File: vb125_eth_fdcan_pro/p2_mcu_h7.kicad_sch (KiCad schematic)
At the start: 62 parts, among them J1 MEM2061-01-188-00-A, J2 TAGconnect NL, J3 Conn_02x20_Pin, M1 DM-OLED042-647, SW1 KSS331GLFS, U1 STM32H725IGKx, X1 ECX-.327-CDX-1293

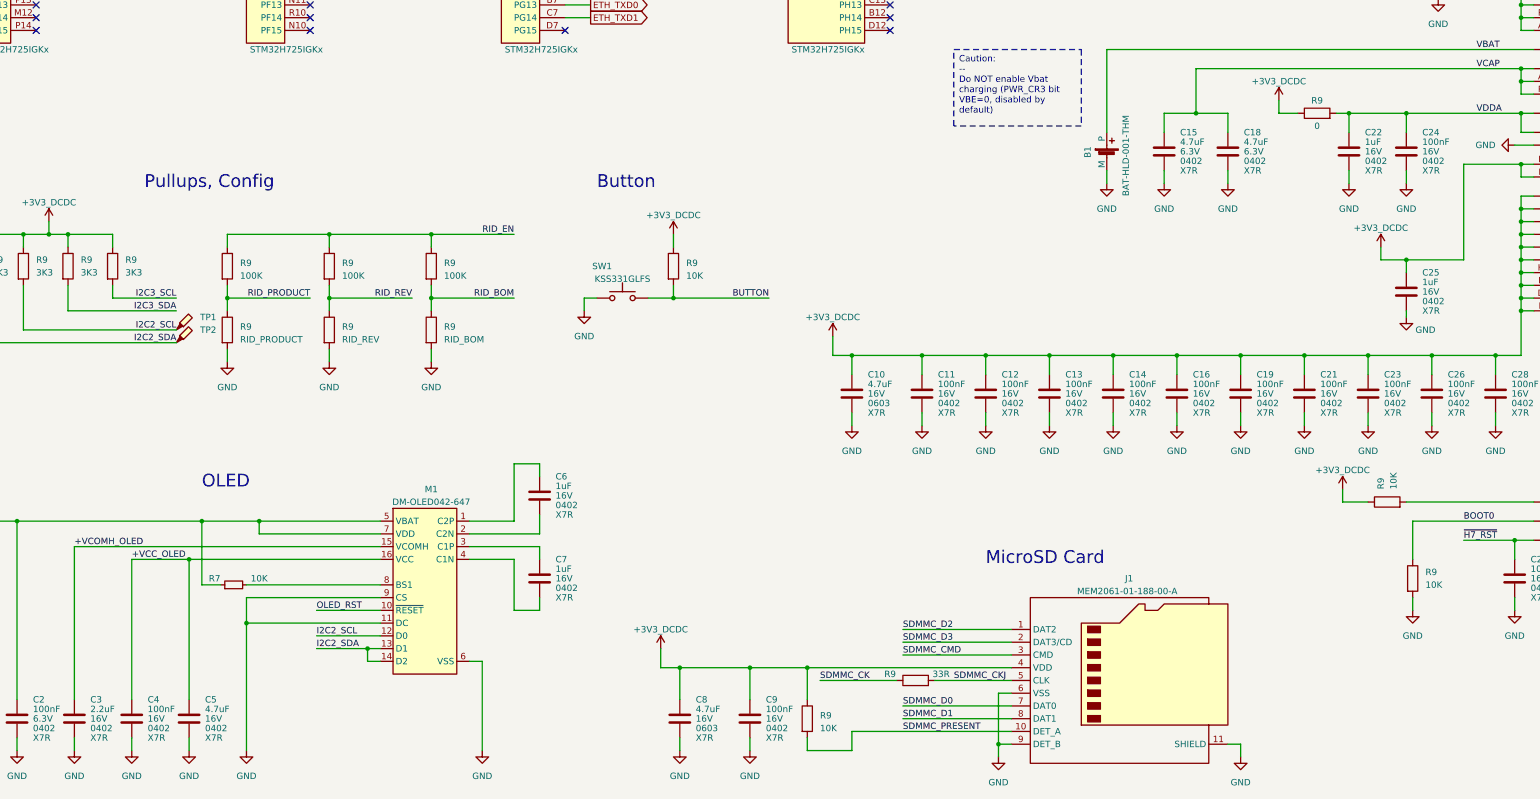
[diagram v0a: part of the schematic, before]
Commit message: Selection of capacitors for VB125
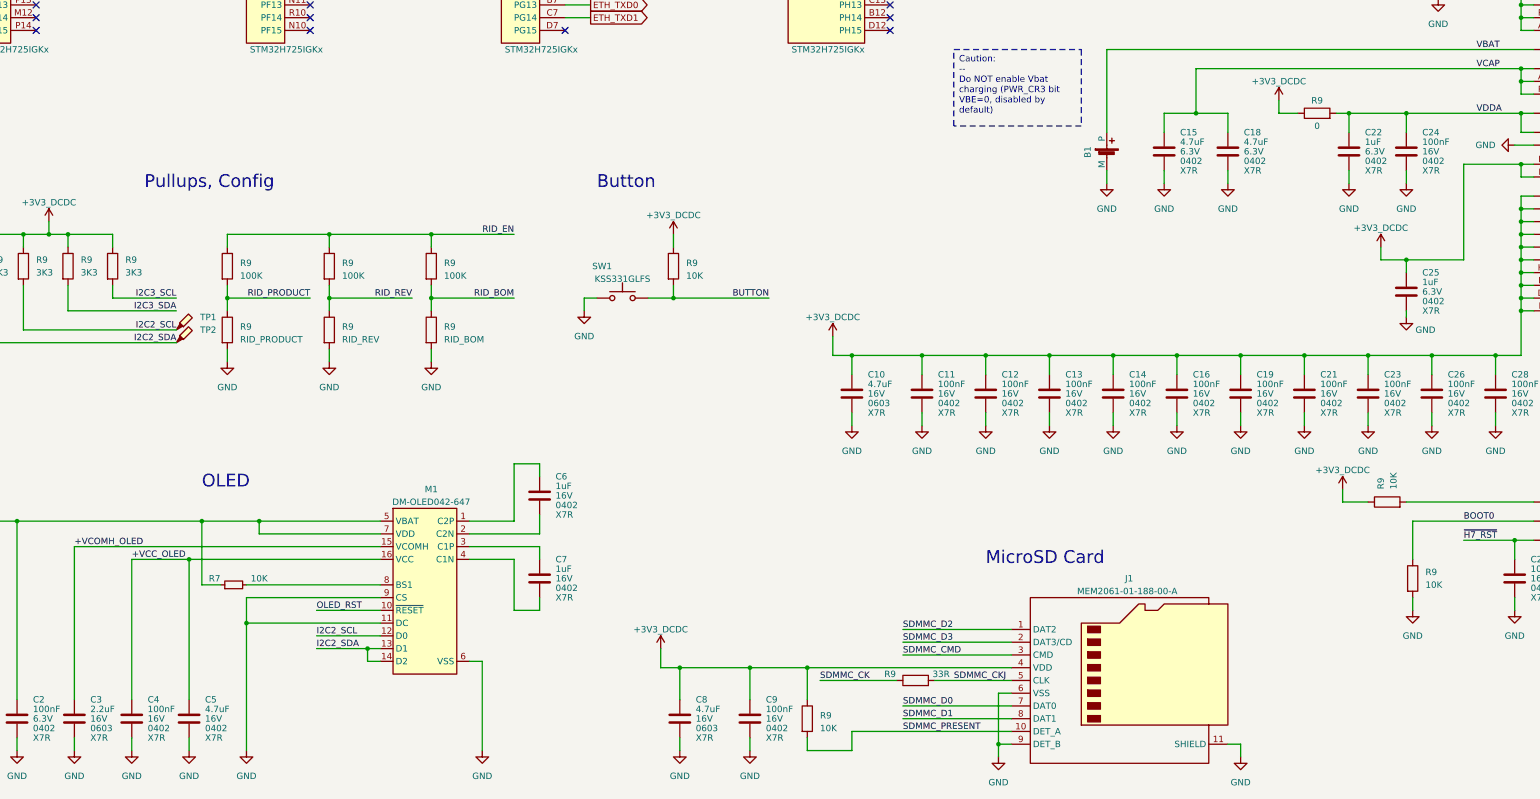
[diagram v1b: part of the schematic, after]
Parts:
- B1: value BAT-HLD-001-THM -> (none)
- C1, C15, C18: Mpn1 (none) -> 06036C475KAT2A; Mpn2 (none) -> ТОЛЬКО ОДИН ПРОИЗВОДИТ. В КОРПУСЕ 0603
- C10, C8: Mpn1 (none) -> Murata:GRM188Z71C475KE21J; Mpn2 (none) -> Murata:GRM188Z71C475KE21D
- C11, C12, C13, C14, C16, C19, C2, C21, C23, C24, C26, C28, C29, C4, C9: Mpn1 (none) -> Samsung:CL05B104KQ5NNNC; Mpn2 (none) -> YAGEO:CC0402KRX7R5BB104
- C17, C20: Mpn1 (none) -> 04025A120KAT2A; Mpn2 (none) -> C0402C120K5GAC7867
- C22, C25: Mpn1 (none) -> Murata:GRM155R70J105KA12D; Mpn2 (none) -> Murata:GRM155R70J105KA12J; Voltage 16V -> 6.3V
- C27, C31: Mpn2 (none) -> - СМОТРЕЛ, В НАЛИЧИИ НЕТ ТАКИХ
- C3: footprint Capacitor_SMD:C_0402_1005Metric -> Capacitor_SMD:C_0603_1608Metric; Mpn1 (none) -> Murata:GRM188Z71C225KE43D; Mpn2 (none) -> Taiyo Yuden:EMK107BB7225KA-T; Package 0402 -> 0603
- C30: Mpn1 (none) -> CC0402KRNPO9BN221; Mpn2 (none) -> C0402C221K5GAC7867
- C6, C7: Mpn1 (none) -> -- mixed values --CL10B105KO8NNNC только В КОРПУСЕ 0603 и б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; Mpn2 (none) -> -- mixed values -- C0603C105K4RAC7867 только В КОРПУСЕ 0603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

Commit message: Add missing footprints, ready to layout.
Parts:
- L1: footprint (none) -> vhrd_inductor:MURATA_LQM2
- X1: footprint vhrd_cristal:ECX-.327-CDX-1293 -> vhrd_crystal:ECX-.327-CDX-1293
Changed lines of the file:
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@@
       (effects (font (size 1.27 1.27)))
     )
-    (property "Footprint" "" (at 387.35 118.11 0)
-      (effects (font (size 1.27 1.27)) hide)
-    )
-    (property "Datasheet" "~" (at 387.35 118.11 0)
+    (property "Footprint" "vhrd_inductor:MURATA_LQM2" (at 387.35 118.11 0)
+      (effects (font (size 1.27 1.27)) hide)
+    )
+    (property "Datasheet" "https://search.murata.co.jp/Ceramy/image/img/P02/JELF243B-0022.pdf" (at 387.35 118.11 0)
       (effects (font (size 1.27 1.27)) hide)
     )
@@
       (effects (font (size 1.27 1.27)))
     )
-    (property "Footprint" "vhrd_cristal:ECX-.327-CDX-1293" (at 281.94 38.1 0)
-      (effects (font (size 1.27 1.27)) hide)
-    )
-    (property "Datasheet" "~https://ecsxtal.com/store/pdf/ECX-.327-CDX-1293.pdf" (at 281.94 35.56 0)
-      (effects (font (size 1.27 1.27)) hide)
-    )
+    (property "Footprint" "vhrd_crystal:ECX-.327-CDX-1293" (at 281.94 38.1 0)
+      (effects (font (size 1.27 1.27)) hide)
+    )
+    (property "Datasheet" "https://ecsxtal.com/store/pdf/ECX-.327-CDX-1293.pdf" (at 281.94 35.56 0)
+      (effects (font (size 1.27 1.27)) hide)
+    )

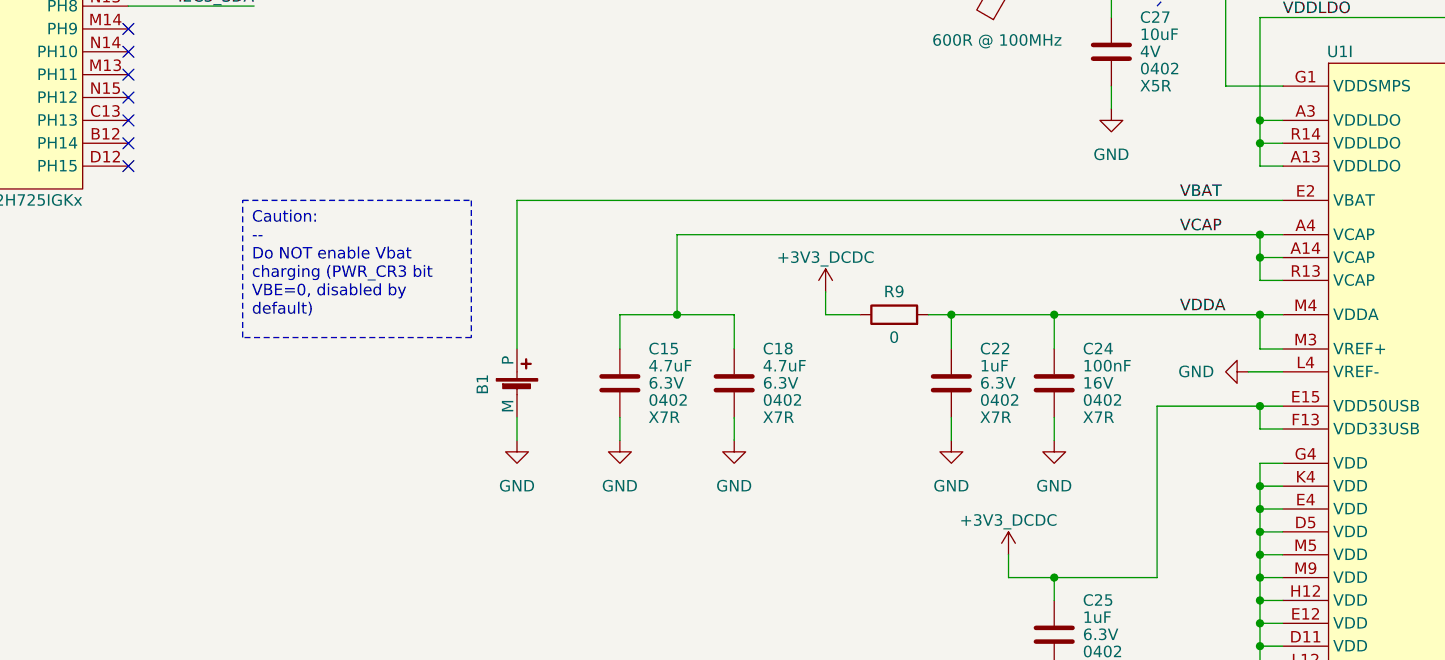
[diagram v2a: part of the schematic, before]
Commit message: Preliminary placement.
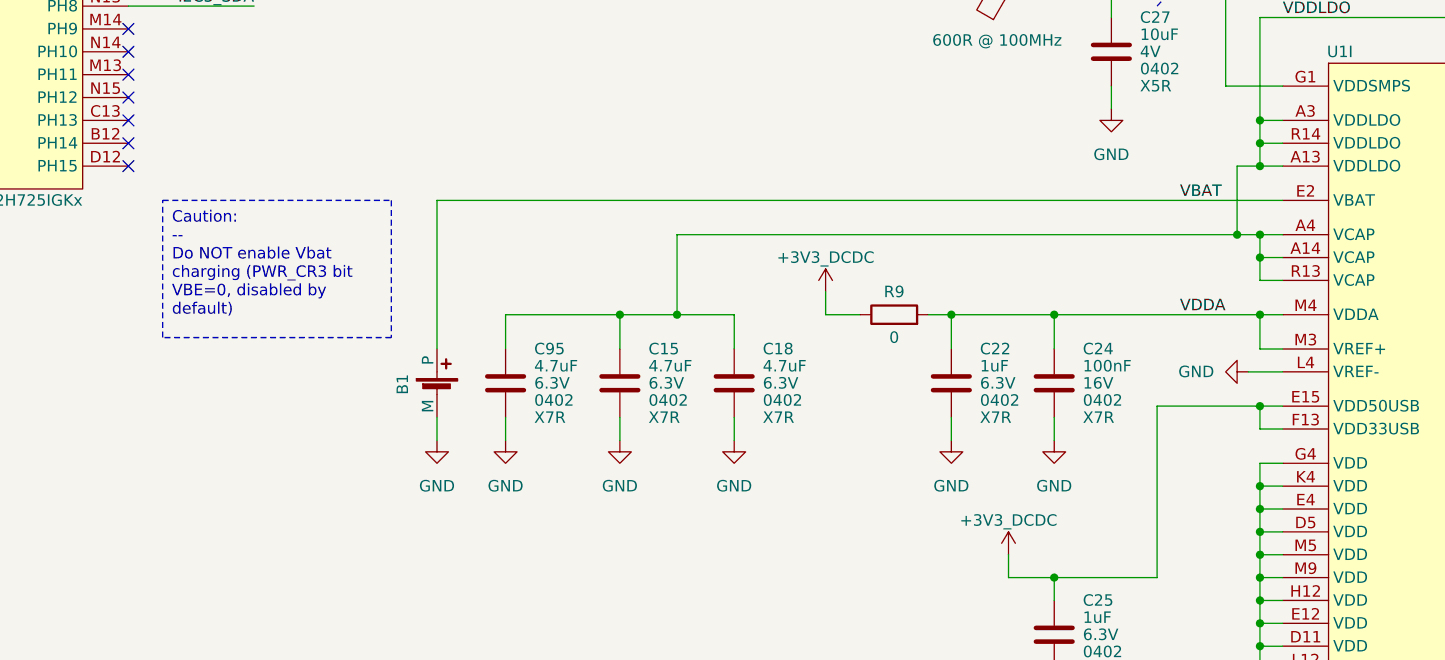
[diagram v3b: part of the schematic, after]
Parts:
- added C95: 4.7uF, Capacitor_SMD:C_0402_1005Metric, symbol Device:C
- M1: footprint vhrd_opto_display:DM-OLED042-647 -> vhrd_opto_display:DM-OLED042-647-TOP
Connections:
- net VCAP is gone; now on net VDDLDO: C15.1, C18.1, U1.A14 (VCAP), U1.A4 (VCAP), U1.R13 (VCAP)
- net GND: now also C95.2
- net VDDLDO: now also C95.1
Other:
- moved on the sheet: B1
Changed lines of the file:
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@@
   (junction (at 311.15 143.51) (diameter 0) (color 0 0 0 0)
   )
+  (junction (at 334.01 127) (diameter 0) (color 0 0 0 0)
+  )
   (junction (at 278.13 191.77) (diameter 0) (color 0 0 0 0)
   )
@@
   (junction (at 350.52 67.31) (diameter 0) (color 0 0 0 0)
   )
+  (junction (at 331.47 134.62) (diameter 0) (color 0 0 0 0)
+  )
   (junction (at 374.65 132.08) (diameter 0) (color 0 0 0 0)
   )
@@
   (junction (at 374.65 200.66) (diameter 0) (color 0 0 0 0)
   )
+  (junction (at 262.89 143.51) (diameter 0) (color 0 0 0 0)
+  )
   (junction (at 334.01 170.18) (diameter 0) (color 0 0 0 0)
   )
@@
     (stroke (width 0) (type default))
   )
+  (wire (pts (xy 250.19 147.32) (xy 250.19 143.51))
+    (stroke (width 0) (type default))
+  )
   (wire (pts (xy 208.28 106.68) (xy 222.25 106.68))
     (stroke (width 0) (type default))
@@
     (stroke (width 0) (type default))
   )
+  (wire (pts (xy 331.47 127) (xy 334.01 127))
+    (stroke (width 0) (type default))
+  )
   (wire (pts (xy 80.01 270.51) (xy 80.01 245.11))
     (stroke (width 0) (type default))
@@
     (stroke (width 0) (type default))
   )
-  (wire (pts (xy 269.24 134.62) (xy 334.01 134.62))
+  (wire (pts (xy 269.24 134.62) (xy 331.47 134.62))
     (stroke (width 0) (type default))
   )
@@
     (stroke (width 0) (type default))
   )
-  (wire (pts (xy 251.46 154.94) (xy 251.46 157.48))
+  (wire (pts (xy 242.57 154.94) (xy 242.57 157.48))
     (stroke (width 0) (type default))
   )
@@
     (stroke (width 0) (type default))
   )
+  (wire (pts (xy 331.47 134.62) (xy 331.47 127))
+    (stroke (width 0) (type default))
+  )
   (wire (pts (xy 38.1 43.18) (xy 71.12 43.18))
     (stroke (width 0) (type default))
@@
     (stroke (width 0) (type default))
   )
-  (wire (pts (xy 251.46 130.81) (xy 336.55 130.81))
+  (wire (pts (xy 242.57 130.81) (xy 336.55 130.81))
     (stroke (width 0) (type default))
   )
@@
     (stroke (width 0) (type default))
   )
+  (wire (pts (xy 250.19 154.94) (xy 250.19 157.48))
+    (stroke (width 0) (type default))
+  )
   (wire (pts (xy 334.01 165.1) (xy 336.55 165.1))
     (stroke (width 0) (type default))
@@
     (stroke (width 0) (type default))
   )
+  (wire (pts (xy 331.47 134.62) (xy 334.01 134.62))
+    (stroke (width 0) (type default))
+  )
   (wire (pts (xy 374.65 139.7) (xy 374.65 137.16))
     (stroke (width 0) (type default))
@@
     (stroke (width 0) (type default))
   )
-  (wire (pts (xy 251.46 130.81) (xy 251.46 147.32))
+  (wire (pts (xy 242.57 130.81) (xy 242.57 147.32))
     (stroke (width 0) (type default))
   )
@@
     (stroke (width 0) (type default))
   )
+  (wire (pts (xy 250.19 143.51) (xy 262.89 143.51))
+    (stroke (width 0) (type default))
+  )
   (wire (pts (xy 273.05 33.02) (xy 273.05 30.48))
     (stroke (width 0) (type default))
@@
   )
   (text_box "Caution:\n--\nDo NOT enable Vbat charging (PWR_CR3 bit VBE=0, disabled by default)"
-    (at 220.98 130.81 0) (size 25.4 15.24)
+    (at 212.09 130.81 0) (size 25.4 15.24)
     (stroke (width 0.1524) (type dash) (color 194 194 0 1))
     (fill (type none))
@@
     (effects (font (size 1.27 1.27) (color 194 0 194 1)) (justify right bottom))
   )
-  (label "VCAP" (at 325.12 134.62 0) (fields_autoplaced)
-    (effects (font (size 1.27 1.27)) (justify left bottom))
-  )
   (label "SPI1_SCK" (at 125.73 35.56 180) (fields_autoplaced)
     (effects (font (size 1.27 1.27) (color 194 0 194 1)) (justify right bottom))
@@
     )
   )
-  (symbol (lib_id "power:GND") (at 251.46 157.48 0) (unit 1)
+  (symbol (lib_id "power:GND") (at 250.19 157.48 0) (unit 1)
+    (in_bom yes) (on_board yes) (dnp no) (fields_autoplaced)
+    (property "Reference" "#PWR09" (at 250.19 163.83 0)
+      (effects (font (size 1.27 1.27)) hide)
+    )
+    (property "Value" "GND" (at 250.19 162.56 0)
+      (effects (font (size 1.27 1.27)))
+    )
+    (property "Footprint" "" (at 250.19 157.48 0)
+      (effects (font (size 1.27 1.27)) hide)
+    )
+    (property "Datasheet" "" (at 250.19 157.48 0)
+      (effects (font (size 1.27 1.27)) hide)
+    )
+    (pin "1")
+    (instances
+      (project "vb125_eth_fdcan_pro"
+        (path "/b473bccb-f14c-41d5-b473-137d3ef8ae1e/c16e79c7-955f-4686-8fe9-acff02e57751"
+          (reference "#PWR09") (unit 1)
+        )
+      )
+    )
+  )
+  (symbol (lib_id "power:GND") (at 242.57 157.48 0) (unit 1)
     (in_bom yes) (on_board yes) (dnp no) (fields_autoplaced)
-    (property "Reference" "#PWR028" (at 251.46 163.83 0)
+    (property "Reference" "#PWR028" (at 242.57 163.83 0)
       (effects (font (size 1.27 1.27)) hide)
     )
-    (property "Value" "GND" (at 251.46 162.56 0)
+    (property "Value" "GND" (at 242.57 162.56 0)
       (effects (font (size 1.27 1.27)))
     )
-    (property "Footprint" "" (at 251.46 157.48 0)
+    (property "Footprint" "" (at 242.57 157.48 0)
       (effects (font (size 1.27 1.27)) hide)
     )
-    (property "Datasheet" "" (at 251.46 157.48 0)
+    (property "Datasheet" "" (at 242.57 157.48 0)
       (effects (font (size 1.27 1.27)) hide)
     )
@@
       (effects (font (size 1.27 1.27)))
     )
-    (property "Footprint" "vhrd_opto_display:DM-OLED042-647" (at 109.22 222.25 0)
+    (property "Footprint" "vhrd_opto_display:DM-OLED042-647-TOP" (at 109.22 222.25 0)
       (effects (font (size 1.27 1.27)) hide)
     )
-    (property "Datasheet" "https://drive.google.com/file/d/1ygmyopC3FinO5EHa4Gdgm3Pccdjo0d4R/view" (at 119.38 257.81 0)
+    (property "Datasheet" "https://cdn.shopify.com/s/files/1/0264/7629/files/DM-OLED042-647_Datasheet_172e9a12-376c-4f72-95bb-83c6a7033324.pdf?v=1675320439" (at 119.38 257.81 0)
       (effects (font (size 1.27 1.27)) hide)
     )
@@
     )
   )
+  (symbol (lib_id "Device:C") (at 250.19 151.13 0) (unit 1)
+    (in_bom yes) (on_board yes) (dnp no)
+    (property "Reference" "C95" (at 253.365 147.32 0)
+      (effects (font (size 1.27 1.27)) (justify left))
+    )
+    (property "Value" "4.7uF" (at 253.365 149.225 0)
+      (effects (font (size 1.27 1.27)) (justify left))
+    )
+    (property "Footprint" "Capacitor_SMD:C_0402_1005Metric" (at 251.1552 154.94 0)
+      (effects (font (size 1.27 1.27)) hide)
+    )
+    (property "Datasheet" "~" (at 250.19 151.13 0)
+      (effects (font (size 1.27 1.27)) hide)
+    )
+    (property "Voltage" "6.3V" (at 253.365 151.13 0)
+      (effects (font (size 1.27 1.27)) (justify left))
+    )
+    (property "Dielectric" "X7R" (at 253.365 154.94 0)
+      (effects (font (size 1.27 1.27)) (justify left))
+    )
+    (property "Package" "0402" (at 253.365 153.035 0)
+      (effects (font (size 1.27 1.27)) (justify left))
+    )
+    (property "Vworking" "?" (at 250.19 151.13 0)
+      (effects (font (size 1.27 1.27)) hide)
+    )
+    (property "Mpn1" "06036C475KAT2A" (at 250.19 151.13 0)
+      (effects (font (size 1.27 1.27)) hide)
+    )
+    (property "Mpn2" "ТОЛЬКО ОДИН ПРОИЗВОДИТ. В КОРПУСЕ 0603" (at 250.19 151.13 0)
+      (effects (font (size 1.27 1.27)) hide)
+    )
+    (pin "1")
+    (pin "2")
+    (instances
+      (project "vb125_eth_fdcan_pro"
+        (path "/b473bccb-f14c-41d5-b473-137d3ef8ae1e/c16e79c7-955f-4686-8fe9-acff02e57751"
+          (reference "C95") (unit 1)
+        )
+      )
+    )
+  )
   (symbol (lib_id "power:GND") (at 180.34 270.51 0) (unit 1)
     (in_bom yes) (on_board yes) (dnp no) (fields_autoplaced)
@@
     )
   )
-  (symbol (lib_id "vhrd_connector_battery:BAT-HLD-001-THM") (at 251.46 152.4 0) (unit 1)
+  (symbol (lib_id "vhrd_connector_battery:BAT-HLD-001-THM") (at 242.57 152.4 0) (unit 1)
     (in_bom yes) (on_board yes) (dnp no)
-    (property "Reference" "B1" (at 247.65 152.4 90)
+    (property "Reference" "B1" (at 238.76 152.4 90)
       (effects (font (size 1.27 1.27)) (justify left))
     )
-    (property "Value" " " (at 255.27 160.02 90)
+    (property "Value" " " (at 246.38 160.02 90)
       (effects (font (size 1.27 1.27)) (justify left))
     )
-    (property "Footprint" "vhrd_connector_battery:BAT-HLD-001-THM" (at 251.46 152.4 0)
+    (property "Footprint" "vhrd_connector_battery:BAT-HLD-001-THM" (at 242.57 152.4 0)
       (effects (font (size 1.27 1.27)) hide)
     )
-    (property "Datasheet" "~https://linxtechnologies.com/wp/wp-content/uploads/bat-hld-001-thm.pdf" (at 251.46 152.4 0)
+    (property "Datasheet" "~https://linxtechnologies.com/wp/wp-content/uploads/bat-hld-001-thm.pdf" (at 242.57 152.4 0)
       (effects (font (size 1.27 1.27)) hide)
     )

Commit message: Continue with floorplan
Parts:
- removed SW1: KSS331GLFS, vhrd_electromechanical:SW_KSS3, symbol Switch:SW_Push
- added VB125C1: vb125c1_button_board, vhrd_boards:vb125c1_button_board, symbol vhrd_boards:vb125c1_button_board
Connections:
- net BUTTON: now also VB125C1.2
- net GND: now also VB125C1.1
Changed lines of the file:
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@@
-    )
-  )
-  (symbol (lib_id "Switch:SW_Push") (at 154.94 180.34 0) (unit 1)
-    (in_bom yes) (on_board yes) (dnp no) (fields_autoplaced)
-    (property "Reference" "SW1" (at 148.9117 173.99 0)
-      (effects (font (size 1.27 1.27)) (justify left))
-    )
-    (property "Value" "KSS331GLFS" (at 154.94 176.53 0)
-      (effects (font (size 1.27 1.27)))
-    )
-    (property "Footprint" "vhrd_electromechanical:SW_KSS3" (at 154.94 175.26 0)
-      (effects (font (size 1.27 1.27)) hide)
-    )
-    (property "Datasheet" "~" (at 154.94 175.26 0)
-      (effects (font (size 1.27 1.27)) hide)
-    )
-    (pin "1")
-    (pin "2")
-    (instances
-      (project "vb125_eth_fdcan_pro"
-        (path "/b473bccb-f14c-41d5-b473-137d3ef8ae1e/c16e79c7-955f-4686-8fe9-acff02e57751"
-          (reference "SW1") (unit 1)
-        )
-      )
     )
   )
@@
         )
       )
+    )
+  )
+  (symbol (lib_id "vhrd_boards:vb125c1_button_board") (at 154.94 180.34 0) (unit 1)
+    (in_bom yes) (on_board yes) (dnp no)
+    (property "Reference" "VB125C1" (at 154.94 175.26 0)
+      (effects (font (size 1.27 1.27)))
+    )
+    (property "Value" "vb125c1_button_board" (at 160.02 182.88 0)
+      (effects (font (size 1.27 1.27)))
+    )
+    (property "Footprint" "vhrd_boards:vb125c1_button_board" (at 154.94 182.88 0)
+      (effects (font (size 1.27 1.27)) hide)
+    )
+    (property "Datasheet" "" (at 154.94 180.34 0)
+      (effects (font (size 1.27 1.27)) hide)
+    )
+    (pin "1")
+    (pin "2")
+    (instances
+      (project "vb125_eth_fdcan_pro"
+        (path "/b473bccb-f14c-41d5-b473-137d3ef8ae1e/c16e79c7-955f-4686-8fe9-acff02e57751"
+          (reference "VB125C1") (unit 1)
+        )
+      )
